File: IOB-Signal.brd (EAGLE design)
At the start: 53.3 x 20.3 mm, 12 parts, among them CON1 RJ45, IC1 74HS139A

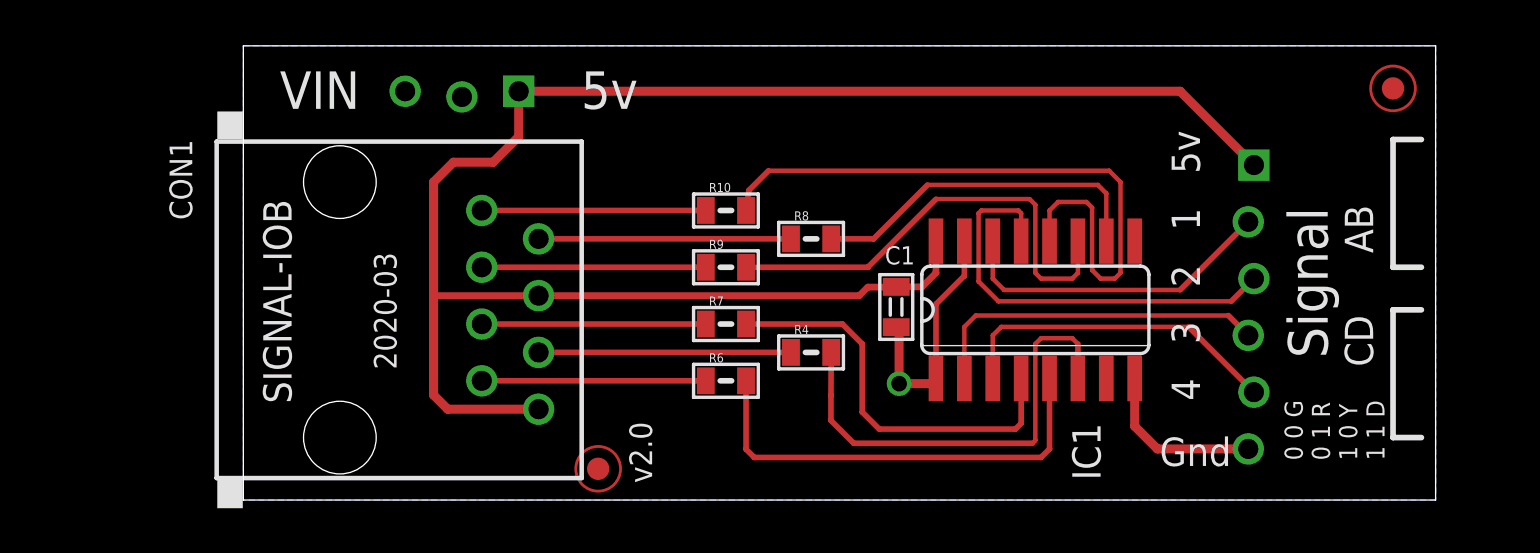
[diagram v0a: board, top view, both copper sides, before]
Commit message: normalized silkscreen layout across IOBs
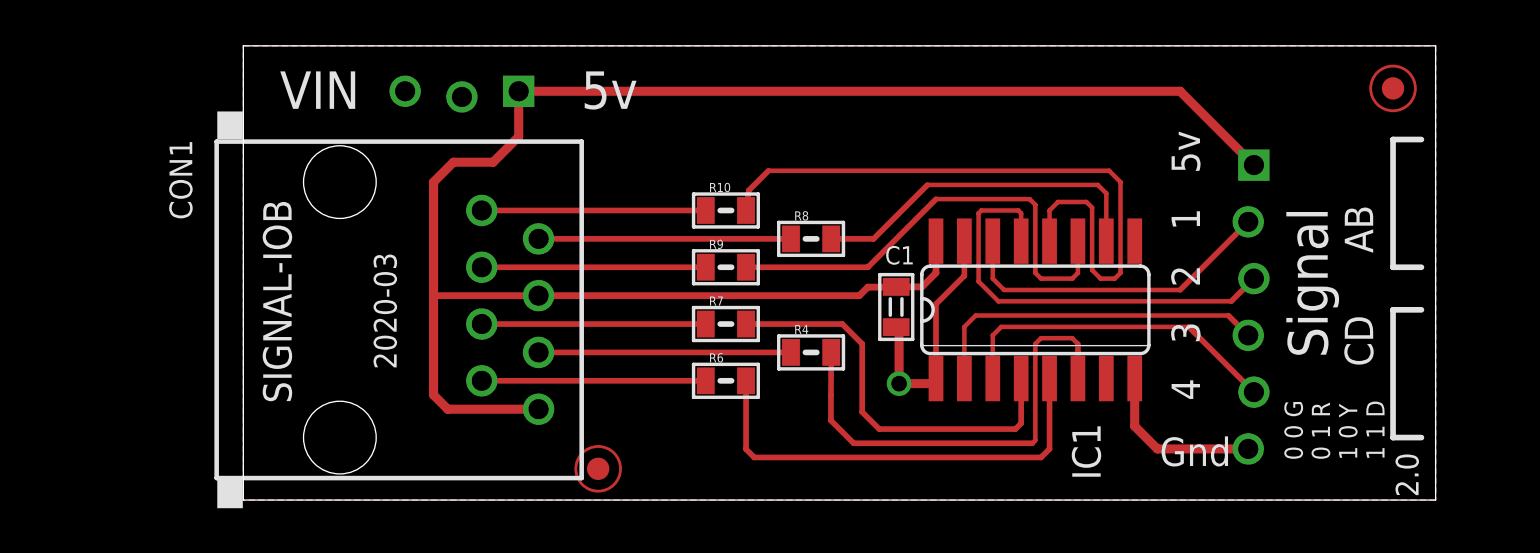
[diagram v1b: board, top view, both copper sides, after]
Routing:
- added copper zone on layer 1, net VCC
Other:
- board text added: "2.0"
- board text added: "Blue Header"
- board text removed: "v2.0"
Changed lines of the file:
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@@
 <layer number="46" name="Milling" color="35" fill="1" visible="yes" active="yes"/>
 <layer number="47" name="Measures" color="21" fill="1" visible="yes" active="yes"/>
-<layer number="48" name="Document" color="36" fill="1" visible="yes" active="yes"/>
+<layer number="48" name="Document" color="15" fill="1" visible="yes" active="yes"/>
 <layer number="49" name="Reference" color="48" fill="1" visible="yes" active="yes"/>
 <layer number="50" name="dxf" color="7" fill="1" visible="no" active="yes"/>
@@
 <layer number="60" name="bCarbon" color="7" fill="1" visible="no" active="no"/>
 <layer number="90" name="Modules" color="5" fill="1" visible="no" active="no"/>
-<layer number="100" name="Muster" color="7" fill="1" visible="no" active="no"/>
-<layer number="101" name="Hidden" color="57" fill="4" visible="yes" active="yes"/>
-<layer number="102" name="Changes" color="13" fill="1" visible="yes" active="yes"/>
-<layer number="103" name="tMap" color="29" fill="4" visible="yes" active="yes"/>
-<layer number="104" name="Name" color="16" fill="1" visible="yes" active="yes"/>
-<layer number="105" name="tPlate" color="7" fill="1" visible="yes" active="yes"/>
-<layer number="106" name="bPlate" color="7" fill="1" visible="yes" active="yes"/>
-<layer number="107" name="Crop" color="7" fill="1" visible="yes" active="yes"/>
-<layer number="108" name="fp8" color="7" fill="1" visible="yes" active="yes"/>
-<layer number="109" name="fp9" color="7" fill="1" visible="yes" active="yes"/>
-<layer number="110" name="fp0" color="7" fill="1" visible="yes" active="yes"/>
-<layer number="111" name="bdokum" color="7" fill="1" visible="yes" active="yes"/>
-<layer number="112" name="tSilk" color="7" fill="1" visible="no" active="no"/>
-<layer number="113" name="IDFDebug" color="7" fill="1" visible="yes" active="yes"/>
-<layer number="114" name="Rect_Pads" color="7" fill="1" visible="yes" active="yes"/>
-<layer number="115" name="_tsilk" color="7" fill="1" visible="yes" active="yes"/>
-<layer number="116" name="Patch_BOT" color="9" fill="4" visible="yes" active="yes"/>
-<layer number="117" name="tTestmark" color="7" fill="1" visible="yes" active="yes"/>
-<layer number="118" name="Rect_Pads" color="7" fill="1" visible="no" active="no"/>
-<layer number="119" name="_tNames" color="7" fill="1" visible="yes" active="yes"/>
-<layer number="120" name="_bNames" color="7" fill="1" visible="yes" active="yes"/>
-<layer number="121" name="_tsilk" color="7" fill="1" visible="yes" active="yes"/>
-<layer number="122" name="_bsilk" color="7" fill="1" visible="yes" active="yes"/>
-<layer number="123" name="tTestmark" color="7" fill="1" visible="yes" active="yes"/>
-<layer number="124" name="bTestmark" color="7" fill="1" visible="yes" active="yes"/>
 <layer number="125" name="_tNames" color="14" fill="1" visible="yes" active="yes"/>
-<layer number="126" name="_bNames" color="7" fill="1" visible="yes" active="yes"/>
-<layer number="127" name="_tValues" color="7" fill="1" visible="no" active="no"/>
-<layer number="128" name="_bValues" color="7" fill="1" visible="no" active="no"/>
-<layer number="129" name="Mask" color="7" fill="1" visible="yes" active="yes"/>
-<layer number="130" name="SMDSTROOK" color="7" fill="1" visible="yes" active="yes"/>
-<layer number="131" name="tAdjust" color="7" fill="1" visible="yes" active="yes"/>
-<layer number="132" name="bAdjust" color="7" fill="1" visible="yes" active="yes"/>
-<layer number="144" name="Drill_legend" color="7" fill="1" visible="yes" active="yes"/>
-<layer number="146" name="Housing" color="7" fill="1" visible="yes" active="yes"/>
-<layer number="147" name="Edge" color="7" fill="1" visible="yes" active="yes"/>
-<layer number="148" name="ReferenceLC" color="7" fill="1" visible="yes" active="yes"/>
-<layer number="149" name="ReferenceLS" color="7" fill="1" visible="yes" active="yes"/>
-<layer number="150" name="Notes" color="7" fill="1" visible="yes" active="yes"/>
-<layer number="151" name="HeatSink" color="7" fill="1" visible="yes" active="yes"/>
-<layer number="152" name="_bDocu" color="7" fill="1" visible="no" active="no"/>
-<layer number="153" name="FabDoc1" color="7" fill="1" visible="yes" active="yes"/>
-<layer number="154" name="FabDoc2" color="7" fill="1" visible="yes" active="yes"/>
-<layer number="155" name="FabDoc3" color="7" fill="1" visible="yes" active="yes"/>
-<layer number="199" name="Contour" color="7" fill="1" visible="yes" active="yes"/>
-<layer number="200" name="200bmp" color="1" fill="10" visible="yes" active="yes"/>
-<layer number="201" name="201bmp" color="2" fill="10" visible="yes" active="yes"/>
-<layer number="202" name="202bmp" color="3" fill="10" visible="yes" active="yes"/>
-<layer number="203" name="203bmp" color="4" fill="10" visible="yes" active="yes"/>
-<layer number="204" name="204bmp" color="5" fill="10" visible="yes" active="yes"/>
-<layer number="205" name="205bmp" color="6" fill="10" visible="yes" active="yes"/>
-<layer number="206" name="206bmp" color="7" fill="10" visible="yes" active="yes"/>
-<layer number="207" name="207bmp" color="8" fill="10" visible="yes" active="yes"/>
-<layer number="208" name="208bmp" color="9" fill="10" visible="yes" active="yes"/>
-<layer number="209" name="209bmp" color="7" fill="1" visible="yes" active="yes"/>
-<layer number="210" name="210bmp" color="7" fill="1" visible="yes" active="yes"/>
-<layer number="211" name="211bmp" color="12" fill="1" visible="no" active="no"/>
-<layer number="212" name="212bmp" color="13" fill="1" visible="no" active="no"/>
-<layer number="213" name="213bmp" color="14" fill="1" visible="no" active="no"/>
-<layer number="214" name="214bmp" color="15" fill="1" visible="no" active="no"/>
-<layer number="215" name="215bmp" color="16" fill="1" visible="no" active="no"/>
-<layer number="216" name="216bmp" color="17" fill="1" visible="no" active="no"/>
-<layer number="217" name="217bmp" color="18" fill="1" visible="no" active="no"/>
-<layer number="218" name="218bmp" color="19" fill="1" visible="no" active="no"/>
-<layer number="219" name="219bmp" color="20" fill="1" visible="no" active="no"/>
-<layer number="220" name="220bmp" color="21" fill="1" visible="no" active="no"/>
-<layer number="221" name="221bmp" color="22" fill="1" visible="no" active="no"/>
-<layer number="222" name="222bmp" color="23" fill="1" visible="no" active="no"/>
-<layer number="223" name="223bmp" color="24" fill="1" visible="no" active="no"/>
-<layer number="224" name="224bmp" color="25" fill="1" visible="no" active="no"/>
-<layer number="225" name="225bmp" color="7" fill="1" visible="yes" active="yes"/>
-<layer number="226" name="226bmp" color="7" fill="1" visible="yes" active="yes"/>
-<layer number="227" name="227bmp" color="7" fill="1" visible="yes" active="yes"/>
-<layer number="228" name="228bmp" color="7" fill="1" visible="yes" active="yes"/>
-<layer number="229" name="229bmp" color="7" fill="1" visible="yes" active="yes"/>
-<layer number="230" name="230bmp" color="7" fill="1" visible="yes" active="yes"/>
-<layer number="231" name="231bmp" color="7" fill="1" visible="yes" active="yes"/>
-<layer number="232" name="Eagle3D_PG2" color="7" fill="1" visible="yes" active="yes"/>
-<layer number="233" name="Eagle3D_PG3" color="7" fill="1" visible="yes" active="yes"/>
-<layer number="247" name="wrappinf" color="7" fill="1" visible="yes" active="yes"/>
-<layer number="248" name="Housing" color="7" fill="1" visible="no" active="no"/>
-<layer number="249" name="Edge" color="7" fill="1" visible="no" active="no"/>
-<layer number="250" name="Descript" color="3" fill="1" visible="no" active="no"/>
-<layer number="251" name="SMDround" color="12" fill="11" visible="no" active="no"/>
-<layer number="252" name="BR-BS" color="7" fill="1" visible="yes" active="yes"/>
-<layer number="253" name="BR-LS" color="7" fill="1" visible="yes" active="yes"/>
-<layer number="254" name="cooling" color="7" fill="1" visible="yes" active="yes"/>
-<layer number="255" name="routoute" color="7" fill="1" visible="yes" active="yes"/>
 </layers>
 <board>
@@
 <wire x1="0" y1="0" x2="53.34" y2="0" width="0" layer="20"/>
 <text x="2.159" y="4.318" size="1.27" layer="21" rot="R90">SIGNAL-IOB</text>
-<text x="18.288" y="0.762" size="1.016" layer="21" rot="R90">v2.0</text>
+<text x="52.578" y="0.127" size="1.016" layer="21" rot="R90">2.0</text>
 <text x="8.255" y="16.764" size="1.27" layer="22" rot="MR270">John Plocher</text>
 <text x="48.514" y="6.35" size="1.778" layer="21" rot="R90">Signal</text>
@@
 <text x="50.546" y="11.049" size="1.27" layer="21" rot="R90">AB</text>
 <text x="50.546" y="5.969" size="1.27" layer="21" rot="R90">CD</text>
-<text x="0" y="21.59" size="1.778" layer="48" font="vector" ratio="10">Blue Soldermask
+<text x="-5.08" y="2.54" size="1.27" layer="48" font="vector" ratio="10" rot="R90">Blue Soldermask
 White Silkscreen</text>
 <text x="6.858" y="5.842" size="1.016" layer="21" rot="R90">2020-03</text>
+<text x="55.245" y="3.175" size="1.27" layer="48" font="vector" ratio="10" rot="R90">Blue Header</text>
 <text x="28.702" y="10.541" size="0.8128" layer="125" font="vector">C1</text>
 <text x="-3.302" y="16.129" size="1.016" layer="125" font="vector" rot="R270">CON1</text>
@@
 <wire x1="12.319" y1="18.288" x2="41.91" y2="18.288" width="0.4064" layer="1"/>
 <wire x1="41.91" y1="18.288" x2="45.212" y2="14.986" width="0.4064" layer="1"/>
+<polygon width="0.3048" layer="1" isolate="0.3048">
+<vertex x="0" y="0"/>
+<vertex x="0" y="20.32"/>
+<vertex x="53.34" y="20.32"/>
+<vertex x="53.34" y="0"/>
+</polygon>
 </signal>
 <signal name="P1" class="2">

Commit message: bottom silk alignment
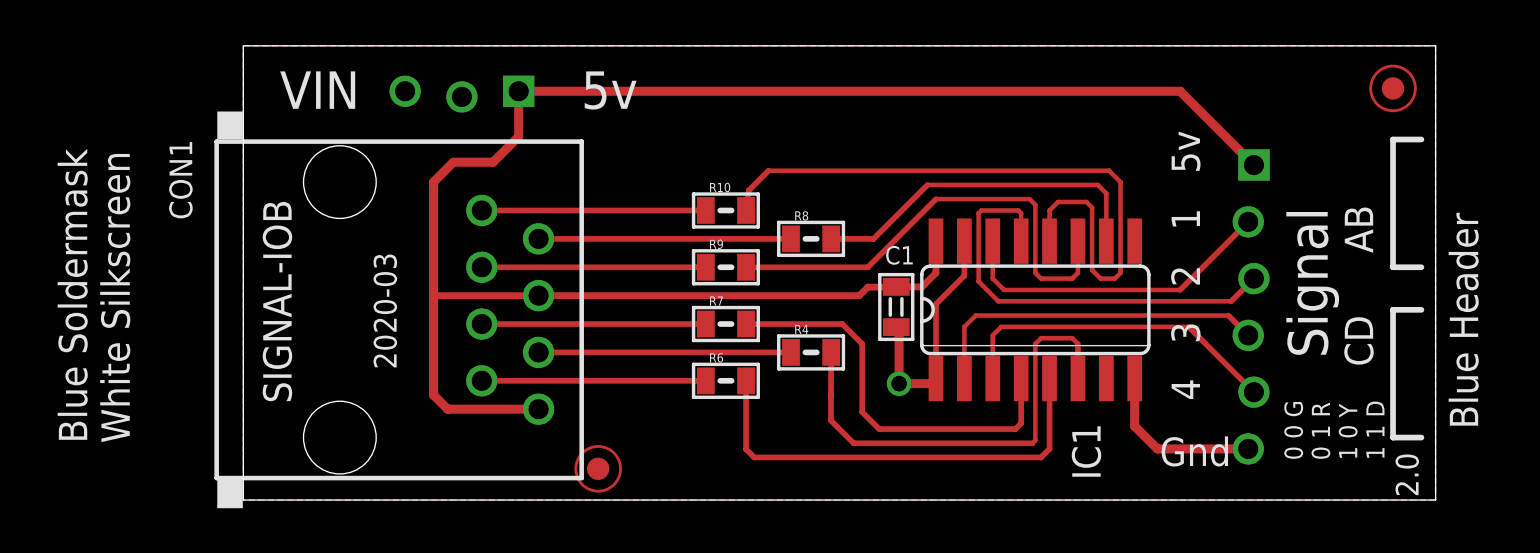
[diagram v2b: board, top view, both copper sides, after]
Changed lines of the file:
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@@
 <text x="50.546" y="11.049" size="1.27" layer="21" rot="R90">AB</text>
 <text x="50.546" y="5.969" size="1.27" layer="21" rot="R90">CD</text>
-<text x="-5.08" y="2.54" size="1.27" layer="48" font="vector" ratio="10" rot="R90">Blue Soldermask
+<text x="-5.08" y="2.54" size="1.27" layer="21" font="vector" ratio="10" rot="R90">Blue Soldermask
 White Silkscreen</text>
 <text x="6.858" y="5.842" size="1.016" layer="21" rot="R90">2020-03</text>
-<text x="55.245" y="3.175" size="1.27" layer="48" font="vector" ratio="10" rot="R90">Blue Header</text>
+<text x="55.245" y="3.175" size="1.27" layer="21" font="vector" ratio="10" rot="R90">Blue Header</text>
 <text x="28.702" y="10.541" size="0.8128" layer="125" font="vector">C1</text>
 <text x="-3.302" y="16.129" size="1.016" layer="125" font="vector" rot="R270">CON1</text>
